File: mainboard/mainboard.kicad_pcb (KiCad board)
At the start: 2 copper layers, 88.9 x 88.9 mm, 46 parts, among them SW1 SW_DPDT_x2, U1 74HC04, U2 AS6C4008, U3 74AC32, U4 74AC00, U5 SST39SF040, U6 NE555, U7 74HC245, U9 74HC574, Y1 Crystal

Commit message: Finshed layout for manifacture
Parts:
- SW1: footprint Button_Switch_THT:SW_CuK_JS202011CQN_DPDT_Straight -> ProjectFootprints:DPDS Switch
- moved SW1 3.56 mm to (137.1, 53.3)
- moved JPOWER1 2.54 mm to (138.4, 66.0)
- moved JPOWER2 2.54 mm to (149.9, 73.7)
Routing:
- net /VIN: track 29.4 -> 35.1 mm
- net +5V: track 275.1 -> 277.3 mm

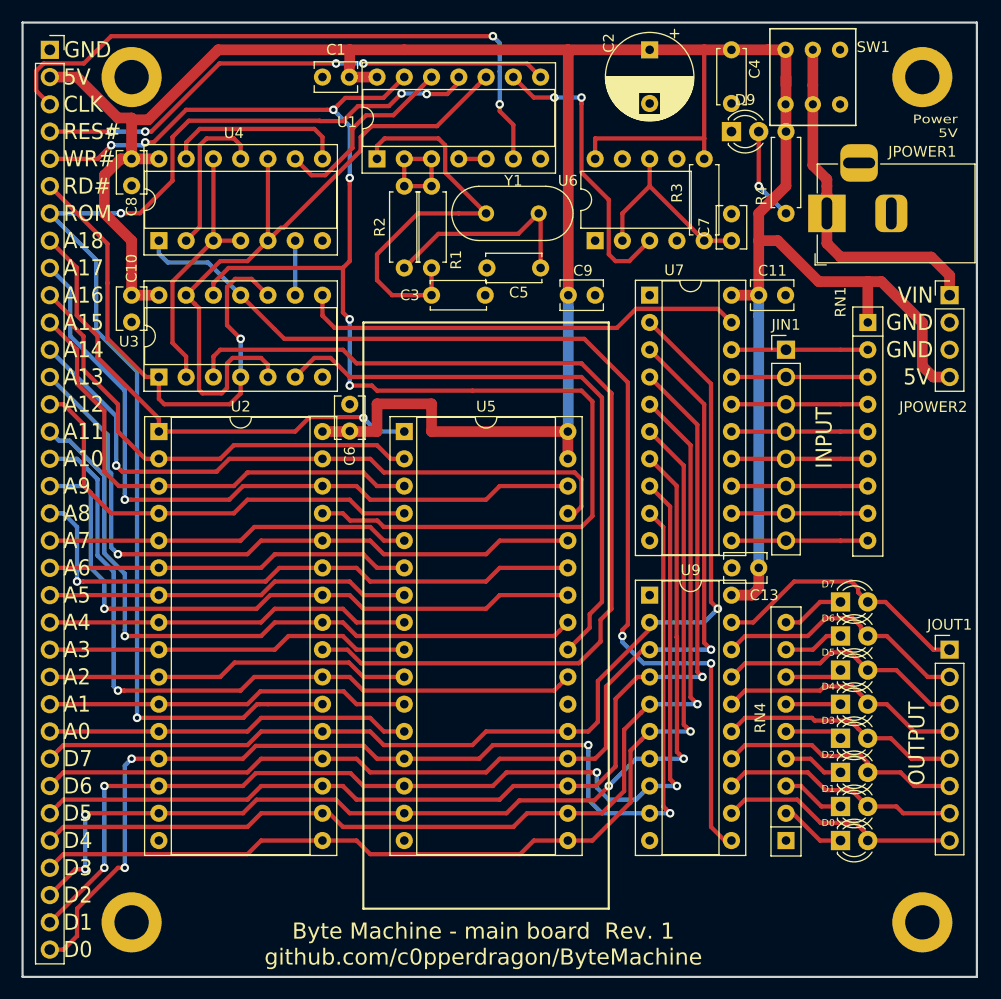
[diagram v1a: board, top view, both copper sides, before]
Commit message: Change mainboard to have larger holes for the ZIF socket and the power switch.
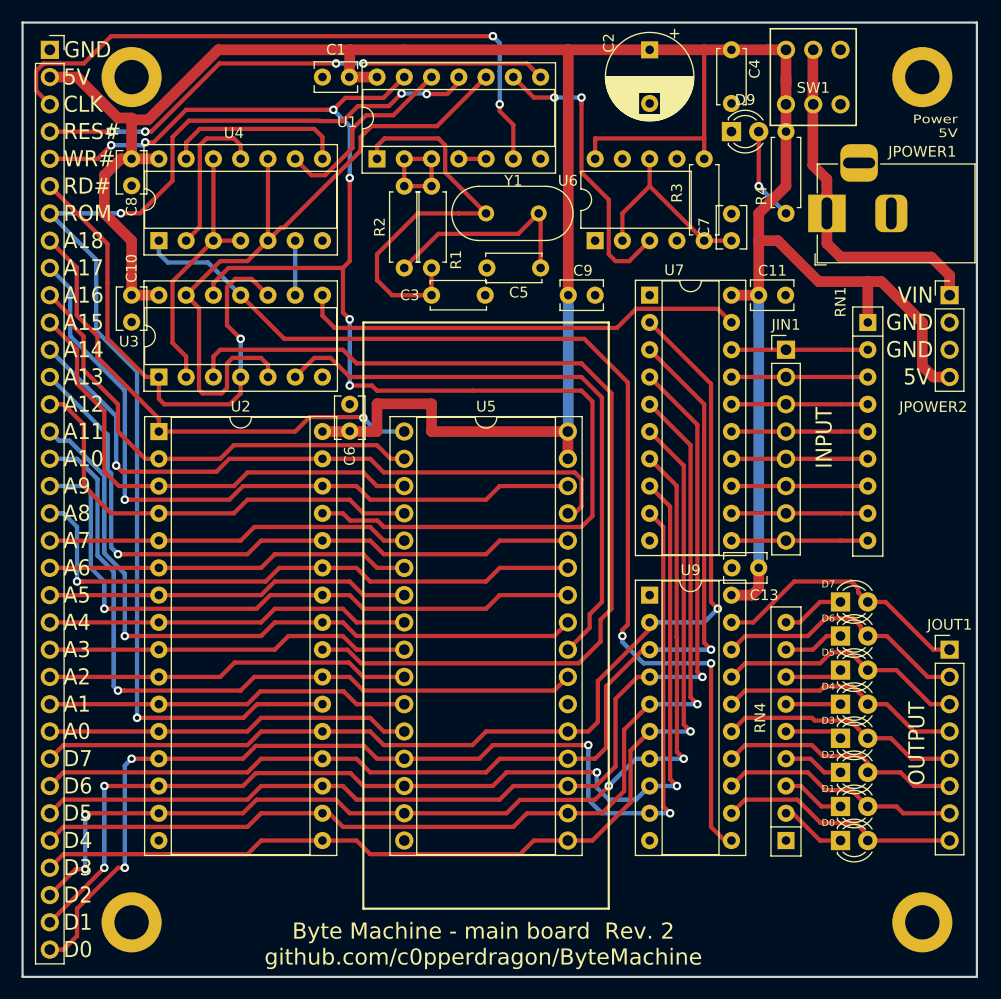
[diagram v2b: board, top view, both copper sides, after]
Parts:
- U5: footprint Package_DIP:DIP-32_W15.24mm_Socket -> ProjectFootprints:DIP-32_LargeHoles
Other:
- board text added: "Byte Machine - main board Rev. 2 github.com/c0pperdragon/ByteMachine"
- board text removed: "Byte Machine - main board Rev. 1 github.com/c0pperdragon/ByteMachine"
